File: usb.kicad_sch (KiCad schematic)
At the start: 108 parts, among them J901 USB-C_GCT_USB4105-GF-A, J902 USB-C_GCT_USB4105-GF-A, Q901 PJE138K, Q902 SQS401EN-T1_BE3, Q903 SSM3J332R, Q904 PJE138K, Q905 PJE138K, Q906 PJE138K, Q907 SQS401EN-T1_BE3, T901 Choke_DLW21SN900SQ2L, T902 Choke_DLW21SN900SQ2L, U901 AP22615A_TSOT26, U902 93AA66C, U903 NCP730BMT330_WSON, U904 NCP730BMT330_WSON, U905 FT4233HPQ, U906 TUSB321RWBR, Y901 Oscillator_SMD_12MHz_KX-7

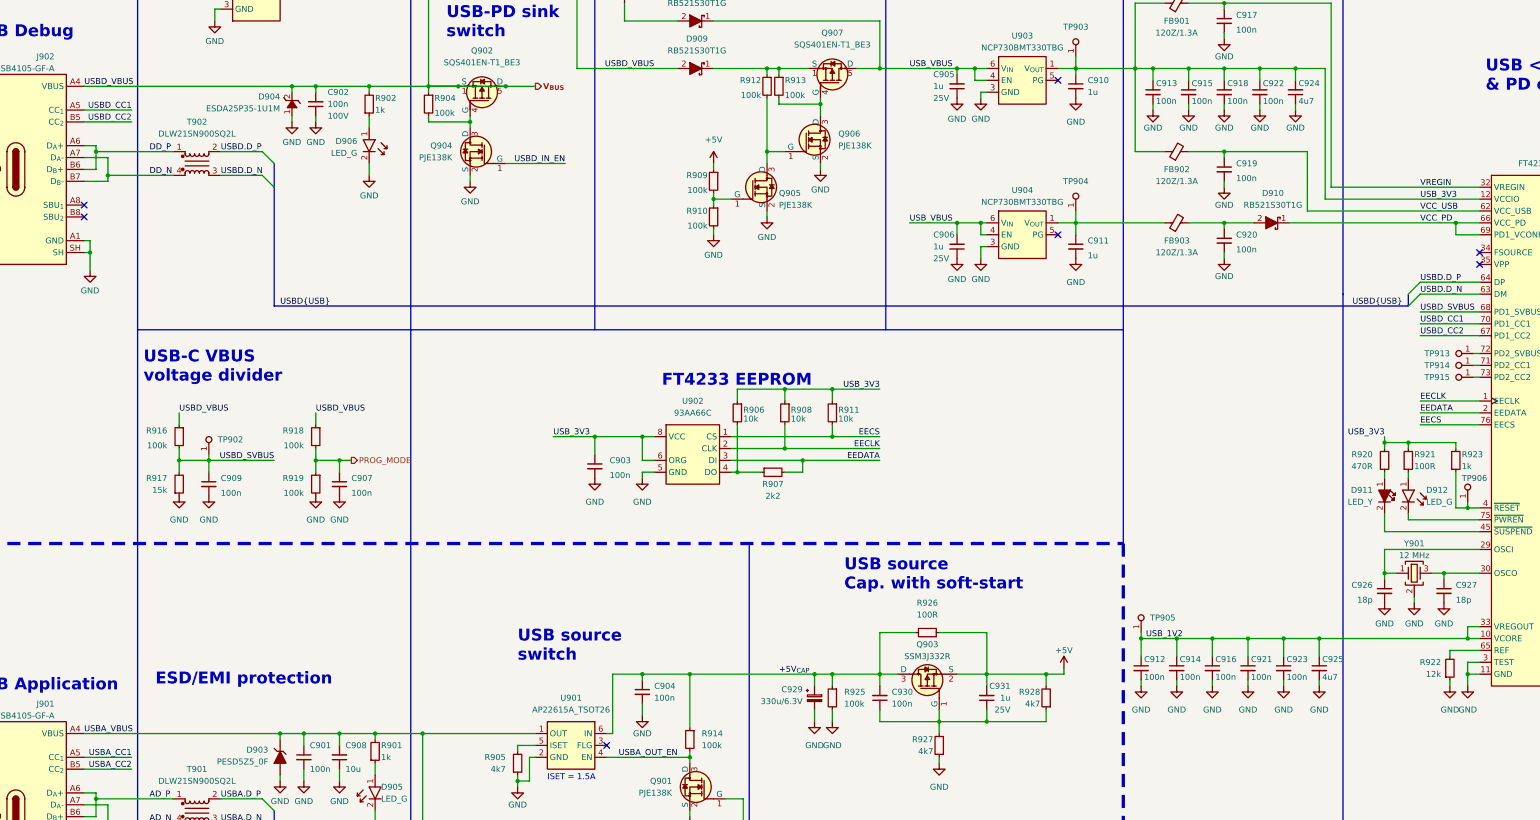
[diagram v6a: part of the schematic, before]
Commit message: [#55181] PCB: USB placement; Sch: minor USB related changes
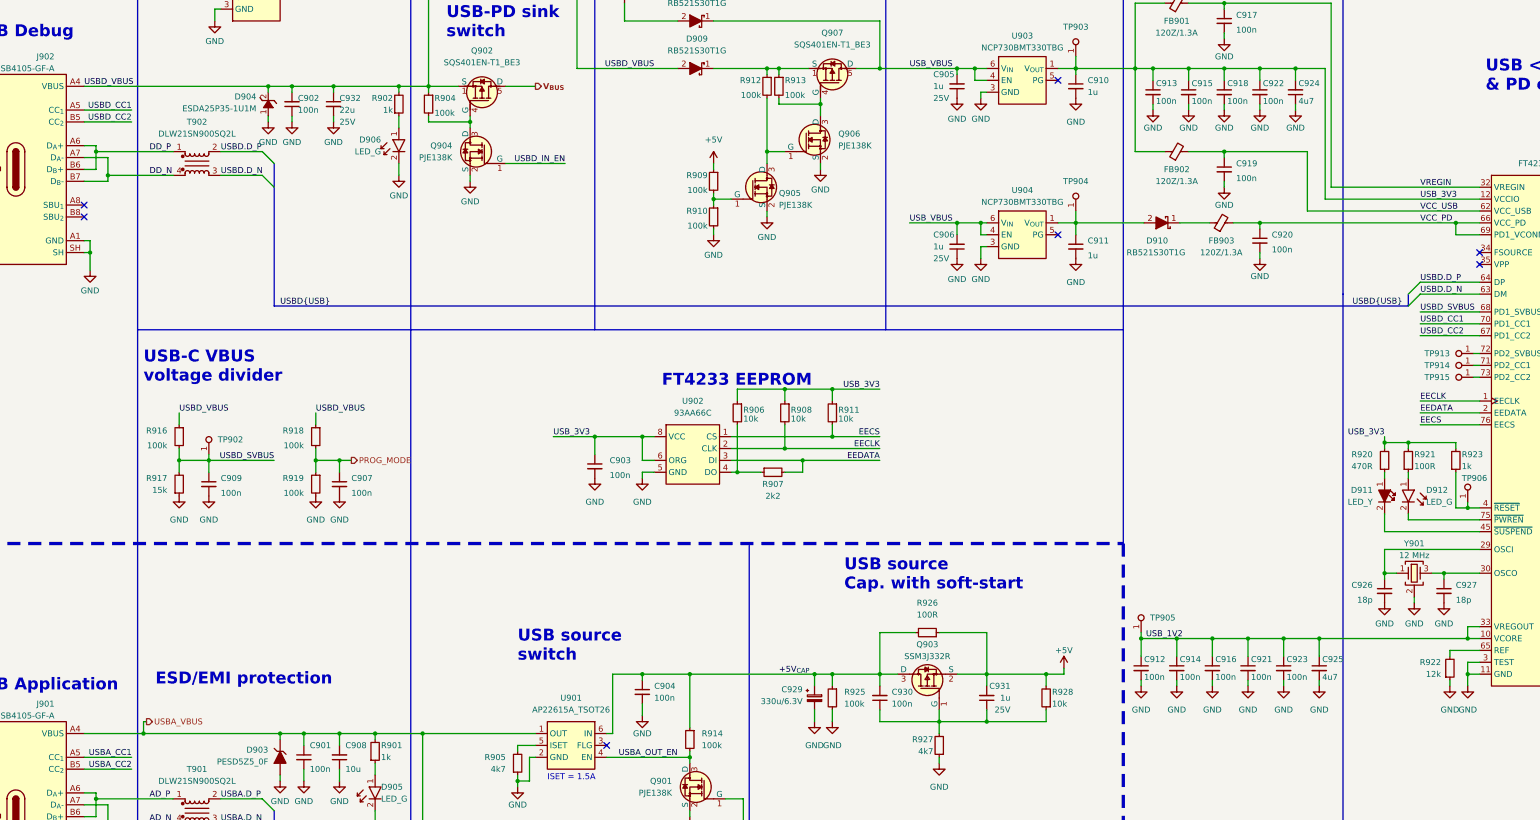
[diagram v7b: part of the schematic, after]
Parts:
- added C932: C_22u_25V_0805, antmicro-footprints:C_0805_2012Metric, symbol antmicroCapacitorsmisc:C_22u_25V_0805
- C902: footprint antmicro-footprints:C_0805_2012Metric -> antmicro-footprints:C_0402_1005Metric; symbol antmicroCapacitorsmisc:C_100n_100V_0805 -> antmicroCapacitors0402:C_100n_0402; Dielectric X7R -> X5R; MPN CL21B104KCFNNNE -> GRM155R61H104KE14D; Manufacturer Samsung Electro-Mechanics -> Murata; Voltage 100V -> 50V
- R928: value R_4k7_0402 -> R_10k_0402; symbol antmicroResistors0402:R_4k7_0402 -> antmicroResistors0402:R_10k_0402; MPN CR0402-FX-4701GLF -> CR0402-FX-1002GLF; Val 4k7 -> 10k
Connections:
- net GND: now also C932.2
- net VCC_PD: now also C920.1, FB903.2; no longer D910.1
- net V_{BUS}: no longer C902.2, D904.2 (A), D909.2, J902.A4 (VBUS), J902.A9 (VBUS), J902.B4 (VBUS), J902.B9 (VBUS), Q902.1 (S), Q902.2 (S), Q902.3 (S), R902.2, R904.1, R916.1, R918.1
- net at C911.1, TP904.1, U904.1 (V_{OUT}): now also D910.2; no longer FB903.1
- new net: D910.1, FB903.1
- new net USBD_VBUS: C902.2, C932.1, D904.2 (A), D909.2, J902.A4 (VBUS), J902.A9 (VBUS), J902.B4 (VBUS), J902.B9 (VBUS), Q902.1 (S), Q902.2 (S), Q902.3 (S), R902.2, R904.1, R916.1, R918.1
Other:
- moved on the sheet: C902, C920, D904, D906, D910, FB903, R902

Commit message: [#55532] Sch: Optimize conections for easier routing
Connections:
- net FT4233.SCL renamed I_{2}C1.SCL
- net FT4233.SDA renamed I_{2}C1.SDA
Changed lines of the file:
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@@
   (no_connect (at 38.1 86.36))
   (no_connect (at 368.3 160.02))
-  (bus_entry (at 383.54 163.83) (size -2.54 2.54)
+  (bus_entry (at 379.73 163.83) (size -2.54 2.54)
     (stroke (width 0) (type default))
   )
@@
     (stroke (width 0) (type default))
   )
+  (bus_entry (at 379.73 166.37) (size -2.54 2.54)
+    (stroke (width 0) (type default))
+  )
   (bus_entry (at 383.54 120.65) (size -2.54 2.54)
     (stroke (width 0) (type default))
@@
     (stroke (width 0) (type default))
   )
-  (bus_entry (at 383.54 166.37) (size -2.54 2.54)
+  (bus_entry (at 383.54 101.6) (size -2.54 2.54)
     (stroke (width 0) (type default))
   )
-  (bus_entry (at 383.54 101.6) (size -2.54 2.54)
+  (bus_entry (at 379.73 166.37) (size -2.54 2.54)
     (stroke (width 0) (type default))
   )
@@
     (stroke (width 0) (type default))
   )
+  (bus_entry (at 379.73 163.83) (size -2.54 2.54)
+    (stroke (width 0) (type default))
+  )
   (bus_entry (at 383.54 144.78) (size -2.54 2.54)
     (stroke (width 0) (type default))
@@
     (stroke (width 0) (type default))
   )
+  (wire (pts (xy 377.19 166.37) (xy 368.3 166.37))
+    (stroke (width 0) (type default))
+  )
   (wire (pts (xy 281.94 78.74) (xy 281.94 80.01))
     (stroke (width 0) (type default))
@@
     (stroke (width 0) (type default))
   )
+  (bus (pts (xy 379.73 162.56) (xy 379.73 163.83))
+    (stroke (width 0) (type default))
+  )
   (wire (pts (xy 110.49 262.89) (xy 129.54 262.89))
     (stroke (width 0) (type default))
@@
     (stroke (width 0) (type default))
   )
-  (bus (pts (xy 383.54 163.83) (xy 383.54 166.37))
-    (stroke (width 0) (type default))
-  )
   (wire (pts (xy 281.94 54.61) (xy 281.94 57.15))
     (stroke (width 0) (type default))
@@
     (stroke (width 0) (type default))
   )
-  (wire (pts (xy 368.3 166.37) (xy 381 166.37))
-    (stroke (width 0) (type default))
-  )
   (wire (pts (xy 330.2 185.42) (xy 330.2 186.69))
     (stroke (width 0) (type default))
@@
     (stroke (width 0) (type default))
   )
-  (wire (pts (xy 368.3 168.91) (xy 381 168.91))
-    (stroke (width 0) (type default))
-  )
   (polyline (pts (xy 307.34 102.87) (xy 307.34 12.7))
     (stroke (width 0) (type default))
@@
     (stroke (width 0) (type default))
   )
+  (wire (pts (xy 377.19 168.91) (xy 368.3 168.91))
+    (stroke (width 0) (type default))
+  )
   (wire (pts (xy 184.15 54.61) (xy 186.69 54.61))
     (stroke (width 0) (type default))
@@
     (stroke (width 0) (type default))
   )
-  (bus (pts (xy 384.81 163.83) (xy 383.54 163.83))
-    (stroke (width 0) (type default))
-  )
   (polyline (pts (xy 307.34 102.87) (xy 307.34 252.73))
     (stroke (width 0) (type default))
@@
     (stroke (width 0) (type default))
   )
+  (bus (pts (xy 381 162.56) (xy 379.73 162.56))
+    (stroke (width 0) (type default))
+  )
   (wire (pts (xy 40.64 72.39) (xy 57.15 72.39))
     (stroke (width 0) (type default))
@@
     (stroke (width 0) (type default))
   )
+  (bus (pts (xy 379.73 163.83) (xy 379.73 166.37))
+    (stroke (width 0) (type default))
+  )
   (wire (pts (xy 184.15 72.39) (xy 187.96 72.39))
     (stroke (width 0) (type default))
@@
     (effects (font (size 1.27 1.27)) (justify right bottom))
   )
-  (label "FT4233.SCL" (at 381 168.91 180) (fields_autoplaced)
-    (effects (font (size 1.27 1.27)) (justify right bottom))
-  )
   (label "USBA_CC2" (at 119.38 259.08 0) (fields_autoplaced)
     (effects (font (size 1.27 1.27)) (justify left bottom))
@@
     (effects (font (size 1.27 1.27)) (justify left bottom))
   )
-  (label "FT4233.SDA" (at 381 166.37 180) (fields_autoplaced)
-    (effects (font (size 1.27 1.27)) (justify right bottom))
-  )
   (label "USBA_OUT_EN" (at 152.4 201.93 0) (fields_autoplaced)
     (effects (font (size 1.27 1.27)) (justify left bottom))
   )
+  (label "I_{2}C1.SCL" (at 377.19 168.91 180) (fields_autoplaced)
+    (effects (font (size 1.27 1.27)) (justify right bottom))
+  )
   (label "USBD.D_P" (at 67.31 72.39 0) (fields_autoplaced)
     (effects (font (size 1.27 1.27)) (justify left bottom))
@@
     (effects (font (size 1.27 1.27)) (justify left bottom))
   )
+  (label "I_{2}C1.SDA" (at 377.19 166.37 180) (fields_autoplaced)
+    (effects (font (size 1.27 1.27)) (justify right bottom))
+  )
   (label "DD_P" (at 57.15 36.83 0) (fields_autoplaced)
     (effects (font (size 1.27 1.27)) (justify left bottom))
@@
     (effects (font (size 1.27 1.27) (thickness 0.254) bold) (justify left))
   )
+  (hierarchical_label "I_{2}C1{I_{2}C}" (shape bidirectional) (at 381 162.56 0) (fields_autoplaced)
+    (effects (font (size 1.27 1.27)) (justify left))
+  )
   (hierarchical_label "USBA_VBUS" (shape output) (at 51.435 194.31 0) (fields_autoplaced)
     (effects (font (size 1.27 1.27)) (justify left))
@@
     (effects (font (size 1.27 1.27)) (justify left))
   )
-  (hierarchical_label "FT4233{I_{2}C}" (shape bidirectional) (at 384.81 163.83 0) (fields_autoplaced)
-    (effects (font (size 1.27 1.27)) (justify left))
-  )
